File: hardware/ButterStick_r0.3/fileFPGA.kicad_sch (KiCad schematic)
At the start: 28 parts, among them U4 ECP5UM5G_85_CABGA381, U5 S25FL127S

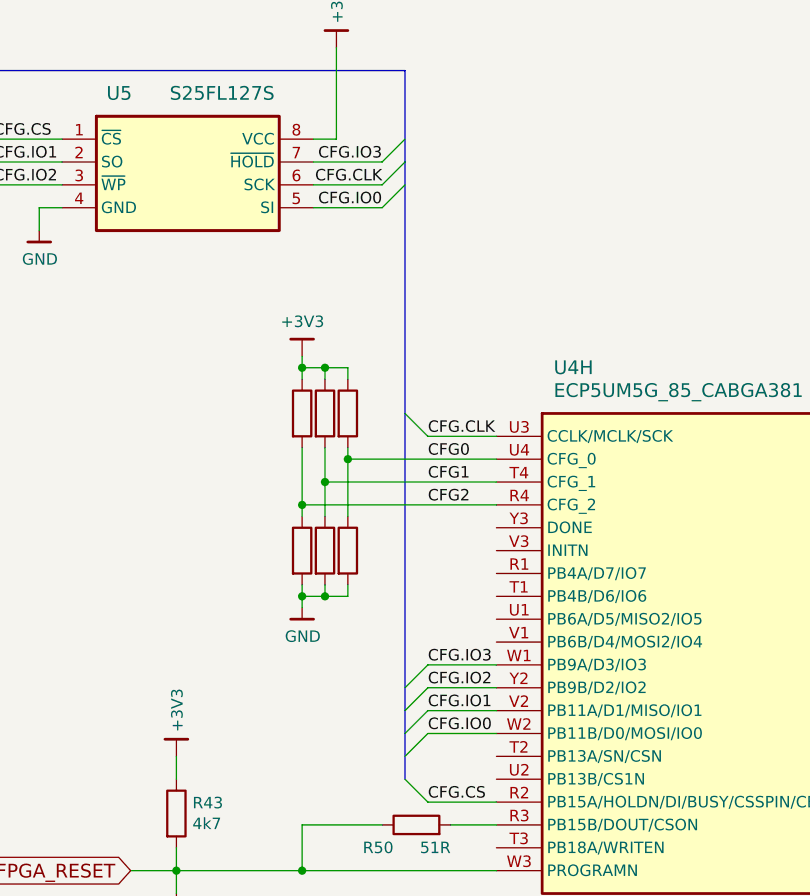
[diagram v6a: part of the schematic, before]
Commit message: hw.r0d3: Continue routing
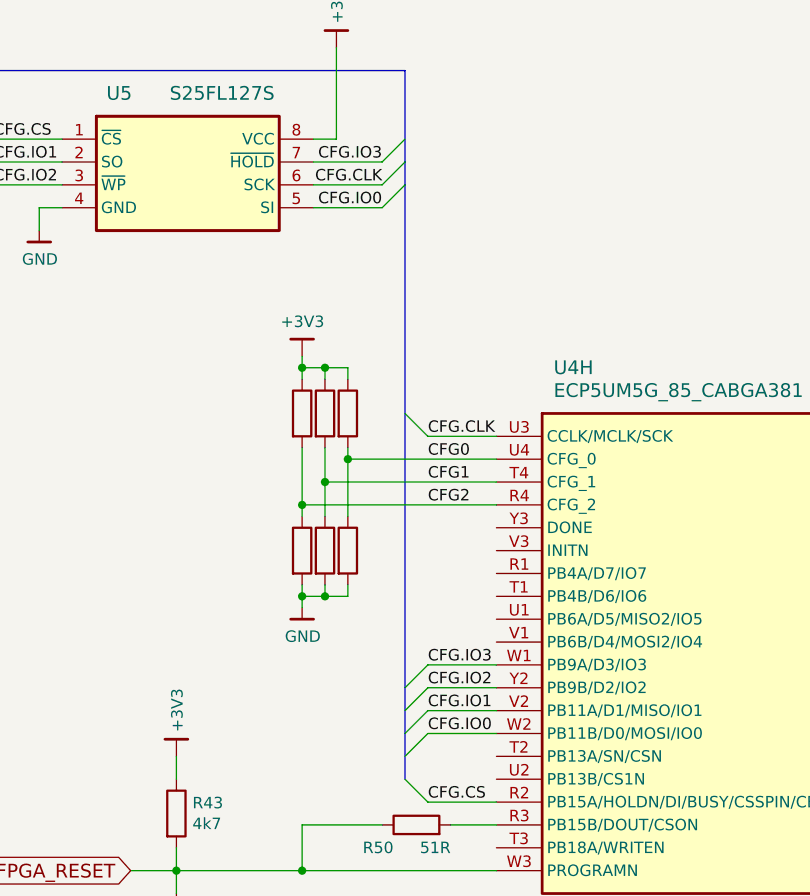
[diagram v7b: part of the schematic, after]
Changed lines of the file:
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@@
 (kicad_sch (version 20200608) (host eeschema "5.99.0-unknown-08c61e6~101~ubuntu18.04.1")
-  (page 1 19)
+  (page 7 19)
   (paper "A4")
   (title_block
@@
     (stroke (width 0) (type solid) (color 0 0 0 0))
   )
-  (bus (pts (xy 74.93 63.5) (xy 74.93 91.44))
-    (stroke (width 0) (type solid) (color 0 0 0 0))
-  )
-  (bus (pts (xy 74.93 91.44) (xy 74.93 124.46))
-    (stroke (width 0) (type solid) (color 0 0 0 0))
-  )
-  (bus (pts (xy 74.93 124.46) (xy 74.93 127))
-    (stroke (width 0) (type solid) (color 0 0 0 0))
-  )
+  (bus (pts (xy 74.93 63.5) (xy 74.93 66.04))
+    (stroke (width 0) (type solid) (color 0 0 0 0))
+  )
+  (bus (pts (xy 74.93 66.04) (xy 74.93 121.92))
+    (stroke (width 0) (type solid) (color 0 0 0 0))
+  )
+  (bus (pts (xy 74.93 121.92) (xy 74.93 127))
+    (stroke (width 0) (type solid) (color 0 0 0 0))
+  )

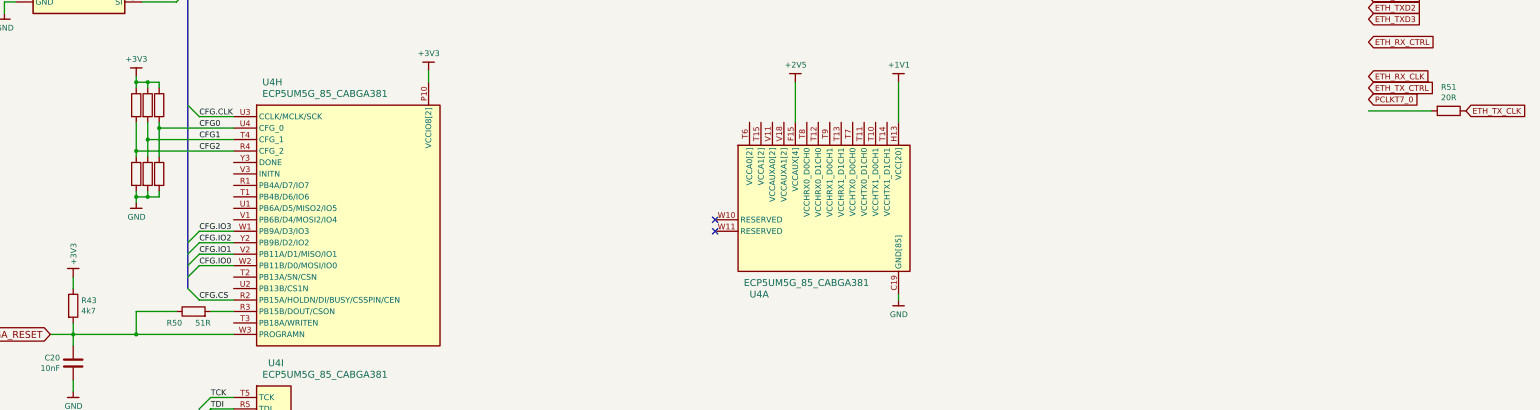
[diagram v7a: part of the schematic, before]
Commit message: hw.r0d3: update DDR3 pinmap and routing
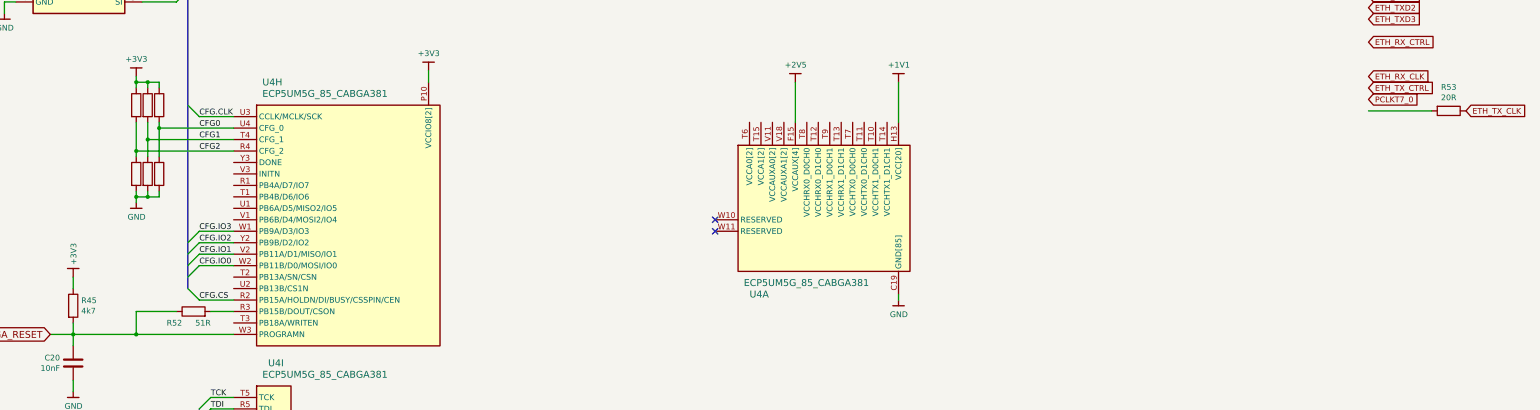
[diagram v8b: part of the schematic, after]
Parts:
- renumbered R43 to R45, R44 to R46, R45 to R47, R46 to R48, R47 to R49, R48 to R50, R49 to R51, R50 to R52, R51 to R53
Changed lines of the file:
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@@
 (kicad_sch (version 20200608) (host eeschema "5.99.0-unknown-08c61e6~101~ubuntu18.04.1")
-  (page 7 19)
+  (page 1 19)
   (paper "A4")
   (title_block
@@
   (symbol (lib_id "gkl_power:GND") (at 34.29 71.12 0) (unit 1)
     (in_bom yes) (on_board yes)
-    (property "Reference" "#PWR062" (id 0) (at 34.29 77.47 0)
+    (property "Reference" "#PWR063" (id 0) (at 34.29 77.47 0)
       (effects (font (size 1.27 1.27)) hide)
     )
@@
   (symbol (lib_id "gkl_power:GND") (at 49.53 154.94 0) (unit 1)
     (in_bom yes) (on_board yes)
-    (property "Reference" "#PWR064" (id 0) (at 49.53 161.29 0)
+    (property "Reference" "#PWR065" (id 0) (at 49.53 161.29 0)
       (effects (font (size 1.27 1.27)) hide)
     )
@@
   (symbol (lib_id "gkl_power:GND") (at 63.5 113.03 0) (unit 1)
     (in_bom yes) (on_board yes)
-    (property "Reference" "#PWR066" (id 0) (at 63.5 119.38 0)
+    (property "Reference" "#PWR067" (id 0) (at 63.5 119.38 0)
       (effects (font (size 1.27 1.27)) hide)
     )
@@
   (symbol (lib_id "gkl_power:GND") (at 232.41 134.62 0) (unit 1)
     (in_bom yes) (on_board yes)
-    (property "Reference" "#PWR071" (id 0) (at 232.41 140.97 0)
+    (property "Reference" "#PWR072" (id 0) (at 232.41 140.97 0)
       (effects (font (size 1.27 1.27)) hide)
     )
@@
   (symbol (lib_id "gkl_power:GND") (at 379.73 73.66 0) (unit 1)
     (in_bom yes) (on_board yes)
-    (property "Reference" "#PWR072" (id 0) (at 379.73 80.01 0)
+    (property "Reference" "#PWR073" (id 0) (at 379.73 80.01 0)
       (effects (font (size 1.27 1.27)) hide)
     )
@@
   (symbol (lib_id "gkl_power:GND") (at 379.73 92.71 0) (unit 1)
     (in_bom yes) (on_board yes)
-    (property "Reference" "#PWR073" (id 0) (at 379.73 99.06 0)
+    (property "Reference" "#PWR074" (id 0) (at 379.73 99.06 0)
       (effects (font (size 1.27 1.27)) hide)
     )
@@
   (symbol (lib_id "gkl_power:GND") (at 389.89 73.66 0) (unit 1)
     (in_bom yes) (on_board yes)
-    (property "Reference" "#PWR074" (id 0) (at 389.89 80.01 0)
+    (property "Reference" "#PWR075" (id 0) (at 389.89 80.01 0)
       (effects (font (size 1.27 1.27)) hide)
     )
@@
   (symbol (lib_id "gkl_power:GND") (at 389.89 92.71 0) (unit 1)
     (in_bom yes) (on_board yes)
-    (property "Reference" "#PWR075" (id 0) (at 389.89 99.06 0)
+    (property "Reference" "#PWR076" (id 0) (at 389.89 99.06 0)
       (effects (font (size 1.27 1.27)) hide)
     )
@@
   (symbol (lib_id "gkl_power:GND") (at 402.59 73.66 0) (unit 1)
     (in_bom yes) (on_board yes)
-    (property "Reference" "#PWR076" (id 0) (at 402.59 80.01 0)
+    (property "Reference" "#PWR077" (id 0) (at 402.59 80.01 0)
       (effects (font (size 1.27 1.27)) hide)
     )
@@
   (symbol (lib_id "gkl_power:GND") (at 402.59 92.71 0) (unit 1)
     (in_bom yes) (on_board yes)
-    (property "Reference" "#PWR077" (id 0) (at 402.59 99.06 0)
+    (property "Reference" "#PWR078" (id 0) (at 402.59 99.06 0)
       (effects (font (size 1.27 1.27)) hide)
     )
@@
   (symbol (lib_id "gkl_power:GND") (at 412.75 73.66 0) (unit 1)
     (in_bom yes) (on_board yes)
-    (property "Reference" "#PWR078" (id 0) (at 412.75 80.01 0)
+    (property "Reference" "#PWR079" (id 0) (at 412.75 80.01 0)
       (effects (font (size 1.27 1.27)) hide)
     )
@@
   (symbol (lib_id "gkl_power:GND") (at 412.75 92.71 0) (unit 1)
     (in_bom yes) (on_board yes)
-    (property "Reference" "#PWR079" (id 0) (at 412.75 99.06 0)
+    (property "Reference" "#PWR080" (id 0) (at 412.75 99.06 0)
       (effects (font (size 1.27 1.27)) hide)
     )
@@
   (symbol (lib_id "gkl_power:GND") (at 426.72 73.66 0) (unit 1)
     (in_bom yes) (on_board yes)
-    (property "Reference" "#PWR080" (id 0) (at 426.72 80.01 0)
+    (property "Reference" "#PWR081" (id 0) (at 426.72 80.01 0)
       (effects (font (size 1.27 1.27)) hide)
     )
@@
   (symbol (lib_id "gkl_power:GND") (at 426.72 92.71 0) (unit 1)
     (in_bom yes) (on_board yes)
-    (property "Reference" "#PWR081" (id 0) (at 426.72 99.06 0)
+    (property "Reference" "#PWR082" (id 0) (at 426.72 99.06 0)
       (effects (font (size 1.27 1.27)) hide)
     )
@@
   (symbol (lib_id "gkl_power:GND") (at 436.88 73.66 0) (unit 1)
     (in_bom yes) (on_board yes)
-    (property "Reference" "#PWR082" (id 0) (at 436.88 80.01 0)
+    (property "Reference" "#PWR083" (id 0) (at 436.88 80.01 0)
       (effects (font (size 1.27 1.27)) hide)
     )
@@
   (symbol (lib_id "gkl_power:GND") (at 436.88 92.71 0) (unit 1)
     (in_bom yes) (on_board yes)
-    (property "Reference" "#PWR083" (id 0) (at 436.88 99.06 0)
+    (property "Reference" "#PWR084" (id 0) (at 436.88 99.06 0)
       (effects (font (size 1.27 1.27)) hide)
     )
@@
   (symbol (lib_id "gkl_power:GND") (at 502.92 -35.56 0) (unit 1)
     (in_bom yes) (on_board yes)
-    (property "Reference" "#PWR084" (id 0) (at 502.92 -29.21 0)
+    (property "Reference" "#PWR085" (id 0) (at 502.92 -29.21 0)
       (effects (font (size 1.27 1.27)) hide)
     )
@@
   (symbol (lib_id "gkl_power:+3V3") (at 49.53 129.54 0) (unit 1)
     (in_bom yes) (on_board yes)
-    (property "Reference" "#PWR063" (id 0) (at 49.53 133.35 0)
+    (property "Reference" "#PWR064" (id 0) (at 49.53 133.35 0)
       (effects (font (size 1.27 1.27)) hide)
     )
@@
   (symbol (lib_id "gkl_power:+3V3") (at 63.5 85.09 0) (unit 1)
     (in_bom yes) (on_board yes)
-    (property "Reference" "#PWR065" (id 0) (at 63.5 88.9 0)
+    (property "Reference" "#PWR066" (id 0) (at 63.5 88.9 0)
       (effects (font (size 1.27 1.27)) hide)
     )
@@
   (symbol (lib_id "gkl_power:+3V3") (at 67.31 50.8 0) (unit 1)
     (in_bom yes) (on_board yes)
-    (property "Reference" "#PWR067" (id 0) (at 67.31 54.61 0)
+    (property "Reference" "#PWR068" (id 0) (at 67.31 54.61 0)
       (effects (font (size 1.27 1.27)) hide)
     )
@@
   (symbol (lib_id "gkl_power:+3V3") (at 128.27 83.82 0) (unit 1)
     (in_bom yes) (on_board yes)
-    (property "Reference" "#PWR068" (id 0) (at 128.27 87.63 0)
+    (property "Reference" "#PWR069" (id 0) (at 128.27 87.63 0)
       (effects (font (size 1.27 1.27)) hide)
     )
@@
   (symbol (lib_id "gkl_power:+2V5") (at 209.55 86.36 0) (unit 1)
     (in_bom yes) (on_board yes)
-    (property "Reference" "#PWR069" (id 0) (at 209.55 90.17 0)
+    (property "Reference" "#PWR070" (id 0) (at 209.55 90.17 0)
       (effects (font (size 1.27 1.27)) hide)
     )
@@
   (symbol (lib_id "gkl_power:+1V1") (at 232.41 86.36 0) (unit 1)
     (in_bom yes) (on_board yes)
-    (property "Reference" "#PWR070" (id 0) (at 232.41 90.17 0)
+    (property "Reference" "#PWR071" (id 0) (at 232.41 90.17 0)
       (effects (font (size 1.27 1.27)) hide)
     )
@@
   (symbol (lib_id "gkl_power:+3V3") (at 505.46 -39.37 270) (mirror x) (unit 1)
     (in_bom yes) (on_board yes)
-    (property "Reference" "#PWR085" (id 0) (at 501.65 -39.37 0)
+    (property "Reference" "#PWR086" (id 0) (at 501.65 -39.37 0)
       (effects (font (size 1.27 1.27)) hide)
     )
@@
   (symbol (lib_id "Device:R") (at 49.53 135.89 0) (unit 1)
     (in_bom yes) (on_board yes)
-    (property "Reference" "R43" (id 0) (at 51.308 134.7216 0)
+    (property "Reference" "R45" (id 0) (at 51.308 134.7216 0)
       (effects (font (size 1.27 1.27)) (justify left))
     )
@@
   (symbol (lib_name "Device:R_3") (lib_id "Device:R") (at 63.5 91.44 0) (unit 1)
     (in_bom yes) (on_board yes)
-    (property "Reference" "R44" (id 0) (at 65.278 90.2716 0)
+    (property "Reference" "R46" (id 0) (at 65.278 90.2716 0)
       (effects (font (size 1.27 1.27)) (justify left) hide)
     )
@@
   (symbol (lib_name "Device:R_5") (lib_id "Device:R") (at 63.5 106.68 0) (unit 1)
     (in_bom yes) (on_board yes)
-    (property "Reference" "R45" (id 0) (at 65.278 105.5116 0)
+    (property "Reference" "R47" (id 0) (at 65.278 105.5116 0)
       (effects (font (size 1.27 1.27)) (justify left) hide)
     )
@@
   (symbol (lib_name "Device:R_2") (lib_id "Device:R") (at 66.04 91.44 0) (unit 1)
     (in_bom yes) (on_board yes)
-    (property "Reference" "R46" (id 0) (at 67.818 90.2716 0)
+    (property "Reference" "R48" (id 0) (at 67.818 90.2716 0)
       (effects (font (size 1.27 1.27)) (justify left) hide)
     )
@@
   (symbol (lib_name "Device:R_6") (lib_id "Device:R") (at 66.04 106.68 0) (unit 1)
     (in_bom yes) (on_board yes)
-    (property "Reference" "R47" (id 0) (at 67.818 105.5116 0)
+    (property "Reference" "R49" (id 0) (at 67.818 105.5116 0)
       (effects (font (size 1.27 1.27)) (justify left) hide)
     )
@@
   (symbol (lib_name "Device:R_1") (lib_id "Device:R") (at 68.58 91.44 0) (unit 1)
     (in_bom yes) (on_board yes)
-    (property "Reference" "R48" (id 0) (at 70.358 90.2716 0)
+    (property "Reference" "R50" (id 0) (at 70.358 90.2716 0)
       (effects (font (size 1.27 1.27)) (justify left) hide)
     )
@@
   (symbol (lib_name "Device:R_4") (lib_id "Device:R") (at 68.58 106.68 0) (unit 1)
     (in_bom yes) (on_board yes)
-    (property "Reference" "R49" (id 0) (at 70.358 105.5116 0)
+    (property "Reference" "R51" (id 0) (at 70.358 105.5116 0)
       (effects (font (size 1.27 1.27)) (justify left) hide)
     )
@@
   (symbol (lib_id "Device:R") (at 76.2 137.16 90) (unit 1)
     (in_bom yes) (on_board yes)
-    (property "Reference" "R50" (id 0) (at 73.66 139.7 90)
+    (property "Reference" "R52" (id 0) (at 73.66 139.7 90)
       (effects (font (size 1.27 1.27)) (justify left))
     )
@@
   (symbol (lib_id "Device:R") (at 354.33 92.71 270) (unit 1)
     (in_bom yes) (on_board yes)
-    (property "Reference" "R51" (id 0) (at 354.33 87.4522 90))
+    (property "Reference" "R53" (id 0) (at 354.33 87.4522 90))
     (property "Value" "20R" (id 1) (at 354.33 89.7636 90))
     (property "Footprint" "Resistor_SMD:R_0402_1005Metric" (id 2) (at 354.33 90.932 90)
